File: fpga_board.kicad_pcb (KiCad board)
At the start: 2 copper layers, 140 x 130 mm, 123 parts, among them J1 Conn_02x20_Odd_Even, J2 FPGA_board, J3 165MDAC, J4 65MADC, J5 65MADC, J6 Conn_01x08, J7 Input, J9 Conn_01x10_Pin, Q1 2N7002H, Q2 2N7002H, Q3 2N7002H, Q4 2N7002H, Q5 2N7002H, Q6 2N7002H, Q7 2N7002H, Q8 2N7002H, SW1 SW_Push, SW10 SW_Push, SW11 SW_DIP_x06, SW12 SW_DIP_x06, SW2 SW_Push, SW3 SW_Push, SW4 SW_Push, SW5 SW_Push, SW6 SW_Push, SW7 SW_Push, SW8 SW_Push, SW9 SW_Push, U1 U, U2 LTV-847, U3 LTV-847, U4 AMS1117-3.3

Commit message: Fix errors with LCD connection
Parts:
- removed R10, R11, R12, R13, R14, R15, R16, R9: 10k, Resistor_SMD:R_1206_3216Metric_Pad1.30x1.75mm_HandSolder
- removed R5, R6: 0, Resistor_SMD:R_1206_3216Metric_Pad1.30x1.75mm_HandSolder
- removed R7, R8: R, Resistor_SMD:R_1206_3216Metric_Pad1.30x1.75mm_HandSolder
- added D8: LED, LED_THT:LED_D3.0mm, F.Cu at (146.9, 87.3)
- J1: moved to B.Cu
- R17, R18, R19, R20, R21, R22: value R -> 330
- R33, R34, R35, R36, R37, R38, R39, R40: value R -> 1k
- R4: value 0 -> 330; moved to B.Cu
- moved R4 93.0 mm to (149.7, 81.0), turned to -90 degrees
- moved J1 48.9 mm to (83.3, 29.6)
- moved R1 25.1 mm to (76.0, 37.0), turned to 180 degrees
- moved R3 15.1 mm to (48.0, 37.0), turned to 0 degrees
- moved R2 10.2 mm to (58.0, 37.0), turned to 0 degrees
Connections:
- J1 pad 1: /N2 -> /V7
- J1 pad 11: /L4 -> /LCD/R0
- J1 pad 12: /L5 -> /LCD/R0
- J1 pad 13: /M5 -> /LCD/R0
- J1 pad 14: /M6 -> /V4
- J1 pad 15: /P3 -> /V2
- J1 pad 16: /LCD/R5 -> /V3
- J1 pad 17: /LCD/R6 -> /U1
- J1 pad 18: /LCD/R7 -> /U2
- J1 pad 19: /T3 -> /LCD/G0
- J1 pad 20: /P4 -> /LCD/G0
- J1 pad 21: /U1 -> /T3
- J1 pad 22: /U2 -> /P4
- J1 pad 23: /V2 -> /T2
- J1 pad 24: /V3 -> /R3
- J1 pad 25: /LCD/G6 -> /P3
- J1 pad 26: /LCD/G7 -> /N4
- J1 pad 27: /U5 -> /LCD/B0
- J1 pad 28: /U6 -> /LCD/B0
- J1 pad 29: /T4 -> /LCD/B0
- J1 pad 30: /R5 -> /M6
- J1 pad 31: /T5 -> /L4
- J1 pad 32: /LCD/B5 -> /L5
- J1 pad 33: /LCD/B6 -> /K5
- J1 pad 34: /LCD/B7 -> /K3
- J1 pad 35: /V6 -> /R1
- J1 pad 36: /U7 -> /P1
- J1 pad 37: /V7 -> /N2
- J1 pad 38: /V8 -> /N1
- J1 pad 4: /N1 -> /V8
- J1 pad 5: /R1 -> /V6
- J1 pad 6: /P1 -> /U7
- J1 pad 7: /K3 -> /R7
- J1 pad 9: /K5 -> /T5
- J6 pad 3: /M2 -> /J5
- J6 pad 4: /J5 -> /M2
- R1 pad 1: /N4 -> GND
- R1 pad 2: /LCD/R5 -> /LCD/R0
- R2 pad 1: /T2 -> GND
- R2 pad 2: /LCD/R6 -> /LCD/G0
- R3 pad 1: /R3 -> GND
- R3 pad 2: /LCD/R7 -> /LCD/B0
- R33 pad 2: /R6 -> /R5
- R34 pad 2: /R3 -> /U4
- R35 pad 2: /T2 -> /U6
- R36 pad 2: /N4 -> /M5
- R37 pad 2: /V4 -> /U5
- R38 pad 2: /U4 -> /T4
- R39 pad 2: /T7 -> /R6
- R4 pad 1: /LCD/B5 -> GND
- R4 pad 2: /R6 -> Net-(D8-K)
- R40 pad 2: /R7 -> /T7
- SW11 pad 10: /J5 -> /M2
- SW11 pad 11: /M2 -> /J5
- SW12 pad 2: /M2 -> /J5
- SW12 pad 3: /J5 -> /M2
- U2 pad 10: /N4 -> /M5
- U2 pad 12: /T2 -> /U6
- U2 pad 14: /R3 -> /U4
- U2 pad 16: /R6 -> /R5
- U3 pad 10: /R7 -> /T7
- U3 pad 12: /T7 -> /R6
- U3 pad 14: /U4 -> /T4
- U3 pad 16: /V4 -> /U5
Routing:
- net /R7: track 245.4 -> 13.5 mm, vias 3 -> 0
- net /V4: track 239.4 -> 12.9 mm, vias 5 -> 0
- net /U5: track 19.6 -> 243.7 mm, vias 0 -> 4
- net /T4: track 18.7 -> 235.8 mm, vias 0 -> 2
- net /R5: track 18.7 -> 210.9 mm, vias 0 -> 2
- net /R3: track 186.3 -> 13.5 mm, vias 3 -> 0
- net /T2: track 174.8 -> 14.1 mm, vias 3 -> 0
- net /U6: track 18.7 -> 174.4 mm, vias 0 -> 2
- net /N4: track 148.7 -> 13.5 mm, vias 5 -> 0
- net /M5: track 18.7 -> 151.0 mm, vias 0 -> 4
- net +5V: track 473.5 -> 397.8 mm, vias 4 -> 1
- net /M1: track 60.9 -> 14.6 mm
- net /U4: track 235.4 -> 190.8 mm, vias 3 -> 2
- net /R6: track 204.8 -> 239.3 mm, vias 3 -> 2
- net /LCD/B7: track 18.5 -> 0.00 mm
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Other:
- board text added: "+"
- board text added: "-"
- board text added: "LED1"
- board text added: "LED1 LED6"
- board text added: "LED2"
- board text added: "LED3"
- board text added: "LED4"
- board text added: "LED5"
- board text added: "LED6"
- board text added: "PB1"
- board text added: "PB10"
- board text added: "PB2"
- board text added: "PB3"
- board text added: "PB4"
- board text added: "PB5"
- board text added: "PB5 PB10"
- board text added: "PB6"
- board text added: "PB7"
- board text added: "PB8"
- board text added: "PB9"

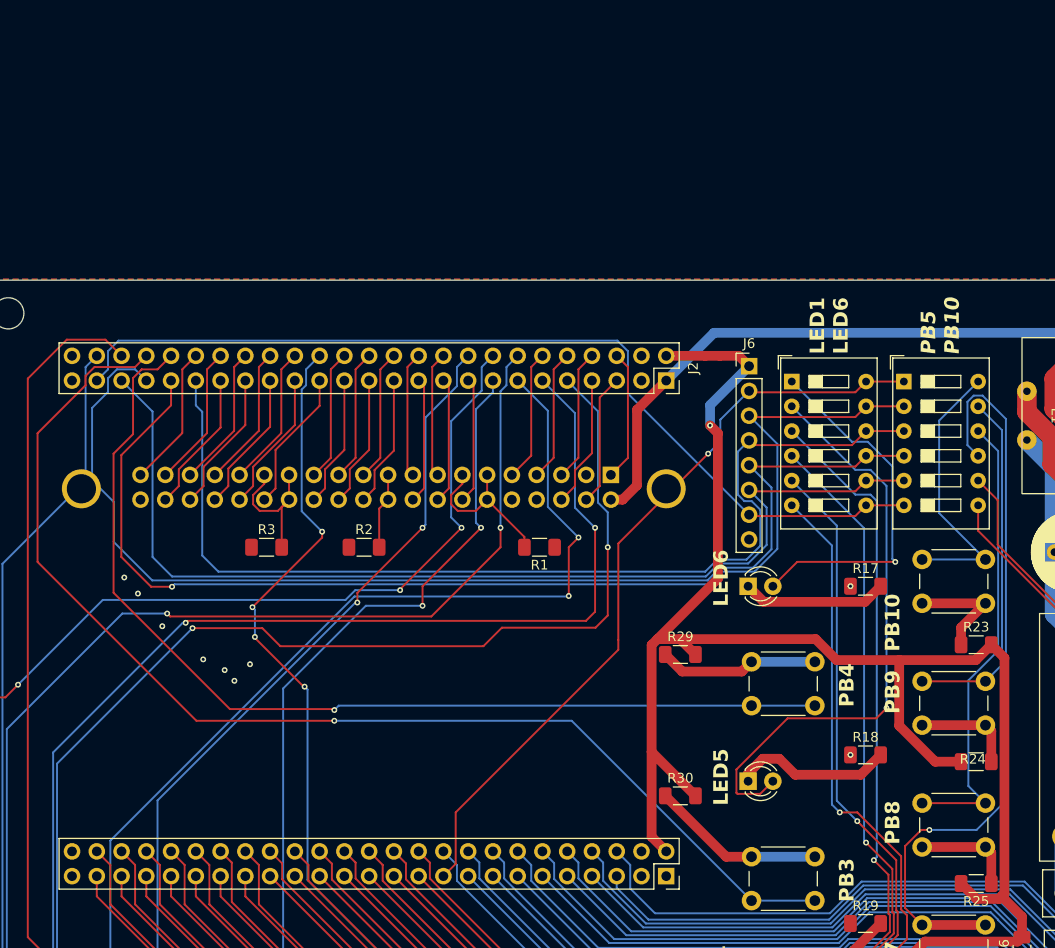
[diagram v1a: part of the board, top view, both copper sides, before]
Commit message: add new type of LCD. start rework pcb
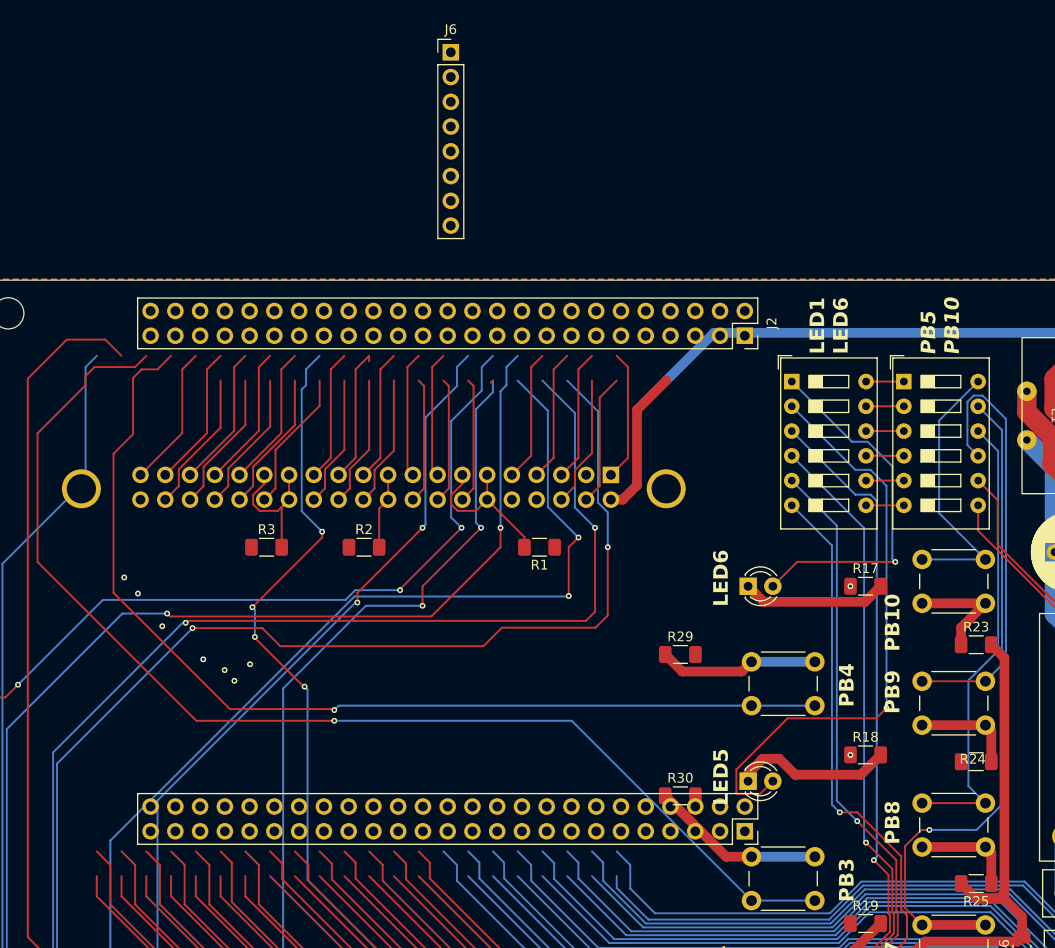
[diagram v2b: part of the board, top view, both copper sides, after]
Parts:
- moved J6 44.4 mm to (66.9, -13.8)
- moved J2 9.28 mm to (97.1, 15.3)
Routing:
- net +3.3V: track 304.0 -> 180.8 mm, vias 11 -> 10
- net /J5: track 121.6 -> 3.88 mm, vias 1 -> 0
- net /J6: track 119.6 -> 3.88 mm
- net /L2: track 107.4 -> 3.88 mm
- net /M2: track 106.6 -> 3.88 mm
- net /K2: track 96.0 -> 3.88 mm
- net /D16: track 79.2 -> 3.88 mm, vias 1 -> 0

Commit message: edit lcd symbol
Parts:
- removed J1: Conn_02x20_Odd_Even, pcbDAC:LCD
- removed R1, R2, R3: 0, Resistor_SMD:R_1206_3216Metric_Pad1.30x1.75mm_HandSolder
- added J8: Conn_02x17_Odd_Even, Connector_PinSocket_2.54mm:PinSocket_2x17_P2.54mm_Vertical, F.Cu at (25.0, 22.6)
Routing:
- net (no net): track 0.00 -> 40.4 mm
- net /LCD/R0: track 16.9 -> 0.00 mm
- net /LCD/B0: track 15.7 -> 0.00 mm
- net /LCD/G0: track 7.80 -> 0.00 mm

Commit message: change logick
на платі будуть роз'єми, цап ацп підключаються плоским кабелем
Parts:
- removed L1: 10mH, PowerLibrary:IndRing
- removed REF** (x4): MountingHole_3.2mm_M3, MountingHole:MountingHole_3.2mm_M3
- removed RV1: 14D560K, eec:Bourns_Inc.-MOV-14D471K-MFG
- removed RV2, RV3: R_Potentiometer, DPAK:TRIM_3296W-1-203
- removed U1: U, PowerLibrary:HLK
- C10, C4, C6, C7, J9, Q1, Q2, Q3, Q4, Q5, Q6, Q7, Q8, R33, R34, R35, R36, R37, R38, R39, R4, R40, R44, R46, R49, R52, R55, R58, R61, R64: moved to F.Cu
- J2: moved to B.Cu
- J3: footprint pcbDAC:165M_DAC -> Connector_PinHeader_2.54mm:PinHeader_2x10_P2.54mm_Vertical; moved to F.Cu
- J4, J5: footprint pcbDAC:65M_ADC -> Connector_PinHeader_2.54mm:PinHeader_2x10_P2.54mm_Vertical; moved to F.Cu
- moved J6 321.5 mm to (376.0, 74.5)
- moved D6 307.8 mm to (396.4, 59.6)
- moved C6 305.6 mm to (432.4, 88.0), turned to 0 degrees
- moved R32 305.5 mm to (393.2, 83.7)
- moved D5 305.2 mm to (396.4, 54.1)
- moved R29 303.8 mm to (393.2, 73.9)
- moved R31 303.6 mm to (393.2, 80.5)
- moved R30 303.1 mm to (393.2, 77.2)
- moved D4 303.1 mm to (396.4, 48.6)
- moved Q7 302.8 mm to (442.0, 61.5)
- moved D3 301.4 mm to (396.4, 43.1)
- moved D2 299.9 mm to (396.4, 37.7)
- moved D1 299.2 mm to (396.4, 32.2)
- moved Q6 294.6 mm to (437.1, 66.1)
- moved Q8 294.6 mm to (442.0, 66.1)
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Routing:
- net +5V: track 397.8 -> 0.00 mm, vias 1 -> 0
- net /U5: track 243.7 -> 0.00 mm, vias 4 -> 0
- net /R6: track 239.3 -> 0.00 mm, vias 2 -> 0
- net /T7: track 237.3 -> 0.00 mm, vias 2 -> 0
- net /T4: track 235.8 -> 0.00 mm, vias 2 -> 0
- net /R5: track 210.9 -> 0.00 mm, vias 2 -> 0
- net /U4: track 190.8 -> 0.00 mm, vias 2 -> 0
- net +3.3V: track 180.8 -> 0.00 mm, vias 10 -> 0
- net /K1: track 174.4 -> 0.00 mm
- net /U6: track 174.4 -> 0.00 mm, vias 2 -> 0
- net /L3: track 163.2 -> 0.00 mm
- net /M5: track 151.0 -> 0.00 mm, vias 4 -> 0
- net Net-(SW10-Pad1): track 148.6 -> 0.00 mm, vias 2 -> 0
- net Net-(SW12-Pad8): track 131.5 -> 0.00 mm, vias 2 -> 0
- net /K6: track 122.3 -> 0.00 mm, vias 1 -> 0
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- removed copper zone on B.Cu, net GND
- removed copper zone on F.Cu, net GND
- removed copper zone on B.Cu, net GND2
- removed copper zone on F.Cu, net GND2
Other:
- board size 140 x 130 mm -> 100 x 100 mm
- board text removed: "+"
- board text removed: "-"
- board text removed: "LED1"
- board text removed: "LED1 LED6"
- board text removed: "LED2"
- board text removed: "LED3"
- board text removed: "LED4"
- board text removed: "LED5"
- board text removed: "LED6"
- board text removed: "PB1"
- board text removed: "PB10"
- board text removed: "PB2"
- board text removed: "PB3"
- board text removed: "PB4"
- board text removed: "PB5"
- board text removed: "PB5 PB10"
- board text removed: "PB6"
- board text removed: "PB7"
- board text removed: "PB8"
- board text removed: "PB9"

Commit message: Make 3d model for ADC and FPGA. Trying to assembly
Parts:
- removed C10: 1uF*50V, Capacitor_SMD:C_1206_3216Metric_Pad1.33x1.80mm_HandSolder
- removed C8, C9: 220uF*10V, Capacitor_THT:CP_Radial_D6.3mm_P2.50mm
- removed J5: 65MADC, Connector_PinHeader_2.54mm:PinHeader_2x10_P2.54mm_Vertical
- removed L2: 10uH, Inductor_SMD:L_6.3x6.3_H3
- removed L3, L4: 1uH, Inductor_SMD:L_6.3x6.3_H3
- added C1: 68uF*35V, Capacitor_Tantalum_SMD:CP_EIA-7361-38_AVX-V_Pad2.18x3.30mm_HandSolder, F.Cu at (138.1, 71.4)
- added C2: 10uF 50V, Capacitor_SMD:C_1210_3225Metric_Pad1.33x2.70mm_HandSolder, F.Cu at (144.7, 62.0)
- added D9: STPS3L40S, Diode_SMD:D_SMC, F.Cu at (127.6, 71.5)
- added J10: Conn_01x02, Connector_PinHeader_2.00mm:PinHeader_1x02_P2.00mm_Vertical, F.Cu at (139.7, 61.9)
- added L1: 27uH, Inductor_SMD:L_Bourns_SRR1208_12.7x12.7mm, F.Cu at (129.9, 60.5)
- added R1: 6.2k, Resistor_SMD:R_0805_2012Metric_Pad1.20x1.40mm_HandSolder, F.Cu at (145.5, 69.1)
- added R2: 13k, Resistor_SMD:R_0805_2012Metric_Pad1.20x1.40mm_HandSolder, F.Cu at (145.5, 72.0)
- added R3: 4.3k, Resistor_SMD:R_0805_2012Metric_Pad1.20x1.40mm_HandSolder, F.Cu at (145.5, 75.0)
- added U1: L5973D013TR, Package_SO:HSOP-8-1EP_3.9x4.9mm_P1.27mm_EP2.41x3.1mm_ThermalVias, F.Cu at (141.9, 56.7)
- C3: value 100uF*50V -> 22pF; footprint Capacitor_THT:CP_Radial_D8.0mm_P3.50mm -> Capacitor_SMD:C_0805_2012Metric_Pad1.18x1.45mm_HandSolder
- C4: value 1uF*50V -> 22nF; footprint Capacitor_SMD:C_1206_3216Metric_Pad1.33x1.80mm_HandSolder -> Capacitor_SMD:C_0805_2012Metric_Pad1.18x1.45mm_HandSolder
- C5: value 100uF*50V -> 22uF; footprint Capacitor_THT:CP_Radial_D8.0mm_P3.50mm -> Capacitor_Tantalum_SMD:CP_EIA-3528-21_Kemet-B_Pad1.50x2.35mm_HandSolder
- C6: value 1uF*50V -> 22uF; footprint Capacitor_SMD:C_1206_3216Metric_Pad1.33x1.80mm_HandSolder -> Capacitor_Tantalum_SMD:CP_EIA-3528-21_Kemet-B_Pad1.50x2.35mm_HandSolder
- C7: value 1nF*250V -> 68uF*35V; footprint Capacitor_SMD:C_1206_3216Metric_Pad1.33x1.80mm_HandSolder -> Capacitor_Tantalum_SMD:CP_EIA-7361-38_AVX-V_Pad2.18x3.30mm_HandSolder
- D7: value SS310 -> STPS2L60
- J2: moved to F.Cu
- J3, J4: footprint Connector_PinHeader_2.54mm:PinHeader_2x10_P2.54mm_Vertical -> Library:CONN-TH_DS1011-20RBSIB7-B
- J8: footprint Connector_PinSocket_2.54mm:PinSocket_2x17_P2.54mm_Vertical -> Connector_PinHeader_2.54mm:PinHeader_2x17_P2.54mm_Horizontal
- moved C4 298.1 mm to (134.4, 92.6)
- moved C7 294.0 mm to (138.5, 83.0)
- moved C6 288.8 mm to (143.6, 92.8)
- moved C3 288.8 mm to (126.1, 92.5)
- moved C5 288.8 mm to (126.1, 102.1)
- moved J7 288.8 mm to (137.0, 107.0)
- moved J3 77.4 mm to (124.9, 123.2), turned to 0 degrees
- moved J4 67.8 mm to (77.4, 123.2), turned to 0 degrees
- moved J8 63.4 mm to (59.2, 80.0), turned to 90 degrees
- moved J2 56.0 mm to (119.5, 64.4), turned to -90 degrees
- moved D7 0.74 mm to (416.3, 103.8)
- moved R4 0.74 mm to (415.2, 107.7)
- moved D8 0.74 mm to (405.3, 108.7)
- moved F1 0.74 mm to (423.5, 108.3)
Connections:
- C3 pad 2: Net-(U1--Vin) -> GND
- C4 pad 2: Net-(U1--Vin) -> Net-(C4-Pad2)
- C5 pad 1: Net-(U1-+Vin) -> +5V
- C5 pad 2: Net-(U1--Vin) -> GND
- C6 pad 1: Net-(U1-+Vin) -> +5V
- C6 pad 2: Net-(U1--Vin) -> GND
- C7 pad 1: Net-(U1--Vin) -> POWER_IN
- C7 pad 2: Net-(U1--Vout) -> GND
- D7 pad 1: /Power/+12vInput -> POWER_IN
- D8 pad 2: +5V -> unconnected-(D8-A-Pad2)
- J7 pad 1: GND1 -> GND
- R4 pad 1: GND -> unconnected-(R4-Pad1)
